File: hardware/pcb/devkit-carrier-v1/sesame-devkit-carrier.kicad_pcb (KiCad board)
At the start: 2 copper layers, 70 x 58 mm, 24 parts, among them J1 DevKit L, J2 DevKit R, J3 OLED, J4 IO, J5 IO2, J6 XT30PW-M, SW1 Switch, U1 Pololu D24V50F5

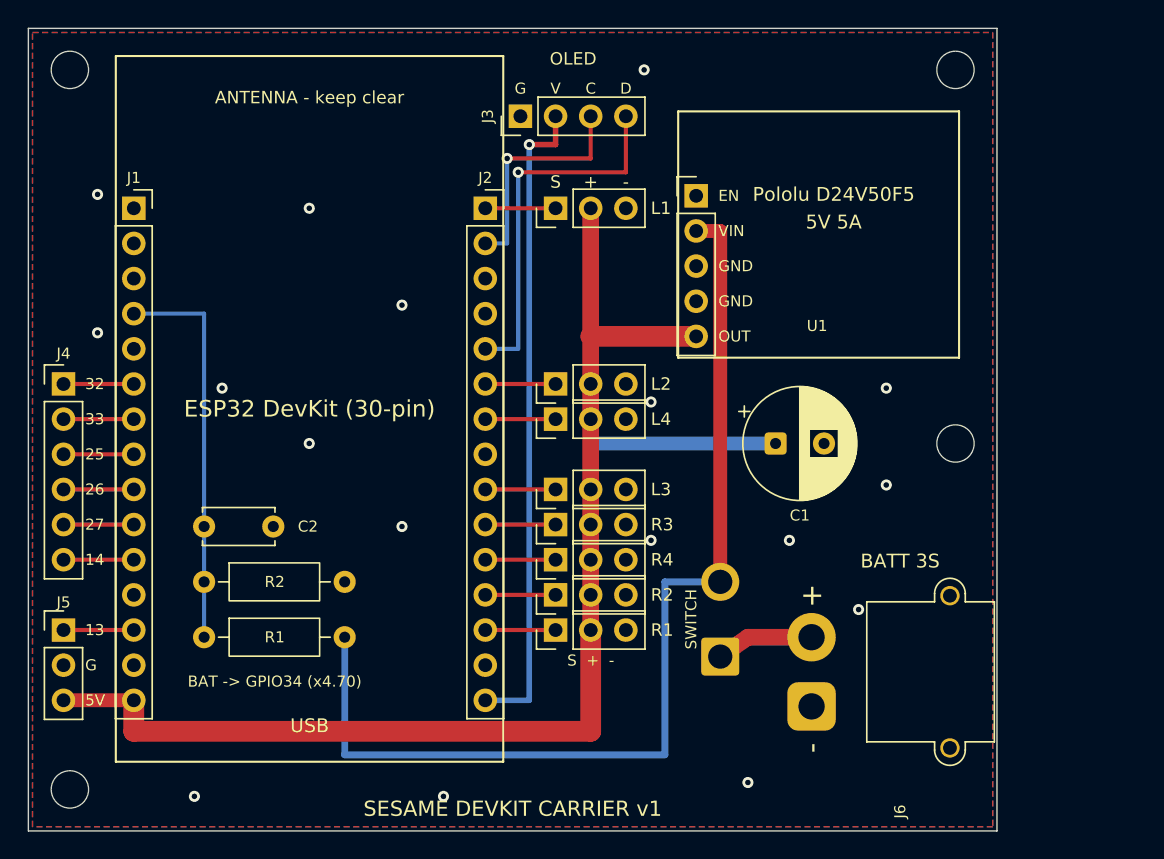
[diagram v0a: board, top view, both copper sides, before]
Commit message: Carrier PCB: 80x42 layout, DevKit USB flush with board edge
DevKit now lies along the board with its micro-USB at the left edge for
flashing; servo headers sit directly under their DevKit pins, spare I/O and
OLED headers along the top edge, power section at the right end.

Co-Authored-By: Claude Opus 5.5 <noreply@anthropic.com>
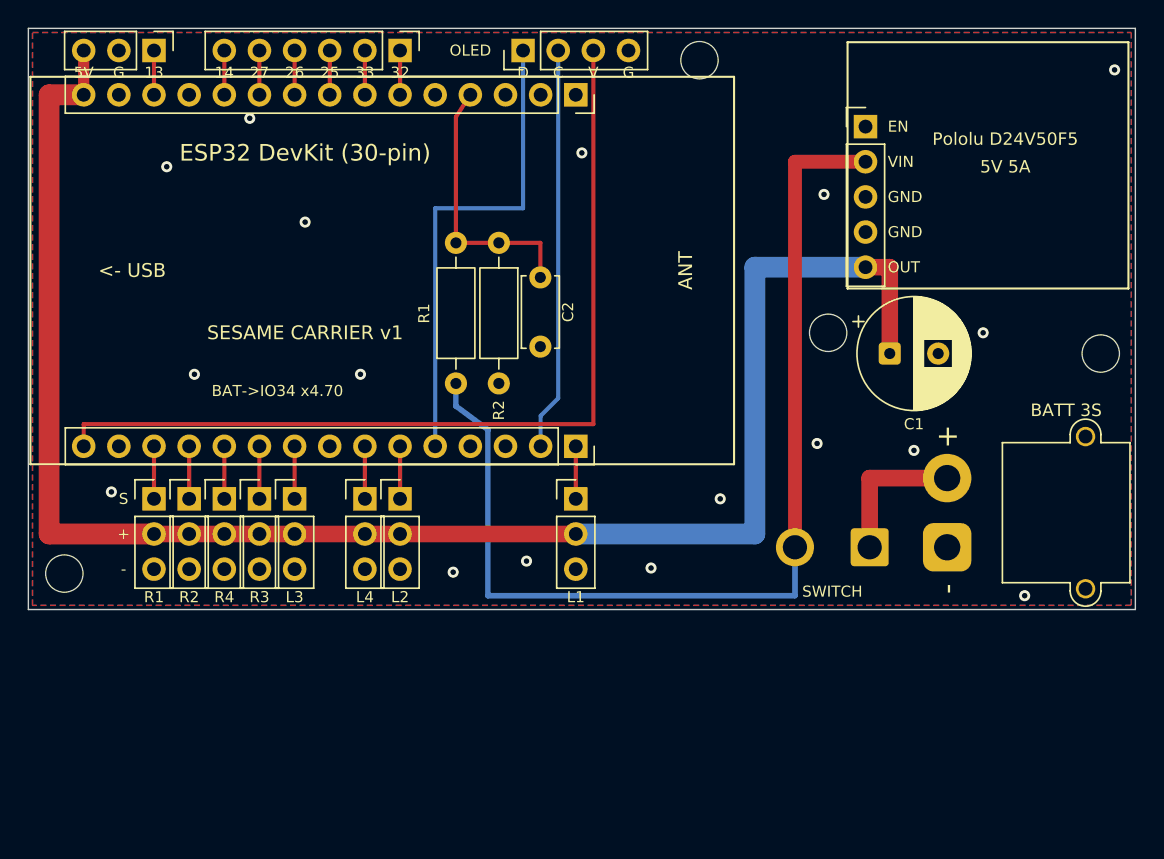
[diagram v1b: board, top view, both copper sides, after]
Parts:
- moved H2 74.0 mm to (2.60, 39.4)
- moved H3 64.0 mm to (57.8, 22.0)
- moved H1 45.5 mm to (48.5, 2.30)
- moved J5 42.4 mm to (9.08, 1.60), turned to -90 degrees
- moved J4 34.2 mm to (26.9, 1.60), turned to -90 degrees
- moved J1 33.0 mm to (39.6, 4.80), turned to -90 degrees
- moved R2 32.5 mm to (34.0, 15.5), turned to -90 degrees
- moved S8 30.5 mm to (9.08, 34.0), turned to 0 degrees
- moved C2 30.2 mm to (37.0, 18.0), turned to -90 degrees
- moved S7 27.4 mm to (11.6, 34.0), turned to 0 degrees
- moved R1 25.8 mm to (30.9, 25.7), turned to 90 degrees
- moved S6 24.3 mm to (14.2, 34.0), turned to 0 degrees
- moved S5 21.5 mm to (16.7, 34.0), turned to 0 degrees
- moved S1 21.1 mm to (39.6, 34.0), turned to 0 degrees
- moved S4 18.9 mm to (19.2, 34.0), turned to 0 degrees
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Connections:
- J3 pad 1: GND -> SDA
- J3 pad 2: +3V3 -> SCL
- J3 pad 3: SCL -> +3V3
- J3 pad 4: SDA -> GND
- R1 pad 1: BAT_SENSE -> VBAT_SW
- R1 pad 2: VBAT_SW -> BAT_SENSE
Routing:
- net +5V: track 100.9 -> 123.7 mm
- net +3V3: track 47.3 -> 65.4 mm, vias 1 -> 0
- net SCL: track 16.8 -> 29.1 mm, vias 1 -> 0
- net BAT_SENSE: track 28.5 -> 19.6 mm
- net SDA: track 27.0 -> 35.0 mm, vias 1 -> 0
- net VBAT: track 7.04 -> 10.6 mm
- net D33: track 5.08 -> 3.20 mm
- net D32: track 5.08 -> 3.20 mm
- net D27: track 5.08 -> 3.20 mm
- net D26: track 5.08 -> 3.20 mm
- net D25: track 5.08 -> 3.20 mm
- net D14: track 5.08 -> 3.20 mm
- net D13: track 5.08 -> 3.20 mm
- net D4: track 5.08 -> 3.80 mm
- net D23: track 5.08 -> 3.80 mm
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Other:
- board size 70 x 58 mm -> 80 x 42 mm
- board text added: "<- USB"
- board text added: "ANT"
- board text added: "BAT->IO34 x4.70"
- board text added: "SESAME CARRIER v1"
- board text removed: "ANTENNA - keep clear"
- board text removed: "BAT -> GPIO34 (x4.70)"
- board text removed: "S + -"
- board text removed: "SESAME DEVKIT CARRIER v1"
- board text removed: "USB"

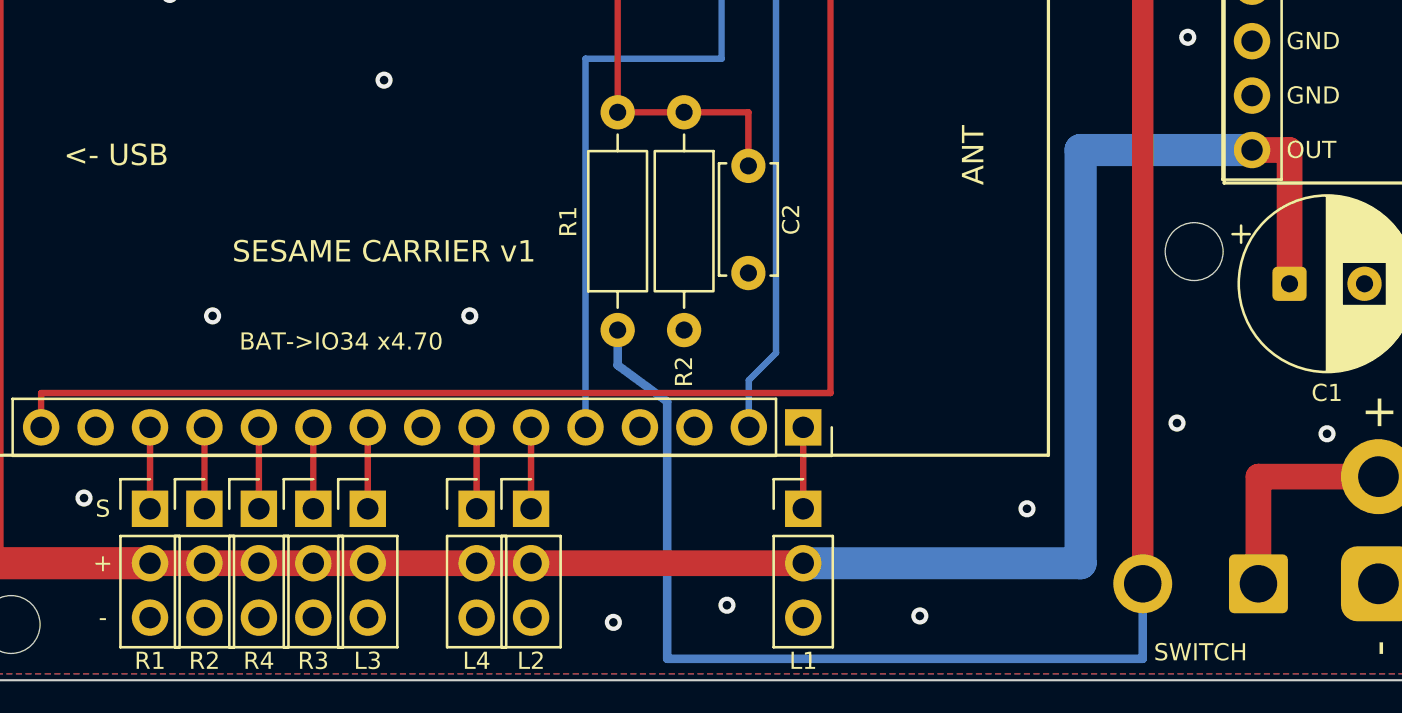
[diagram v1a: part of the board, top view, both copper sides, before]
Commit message: Carrier PCB review fixes: 22k sense resistor, 2mm servo 5V path
R2 27k -> 22k keeps a full 3S pack (12.6 V) at 2.27 V on GPIO34, inside
the ESP32 ADC's accurate range. Servo 5V rail and regulator feed widened
to 2.0 mm for peak servo current.

Co-Authored-By: Claude Opus 5.5 <noreply@anthropic.com>
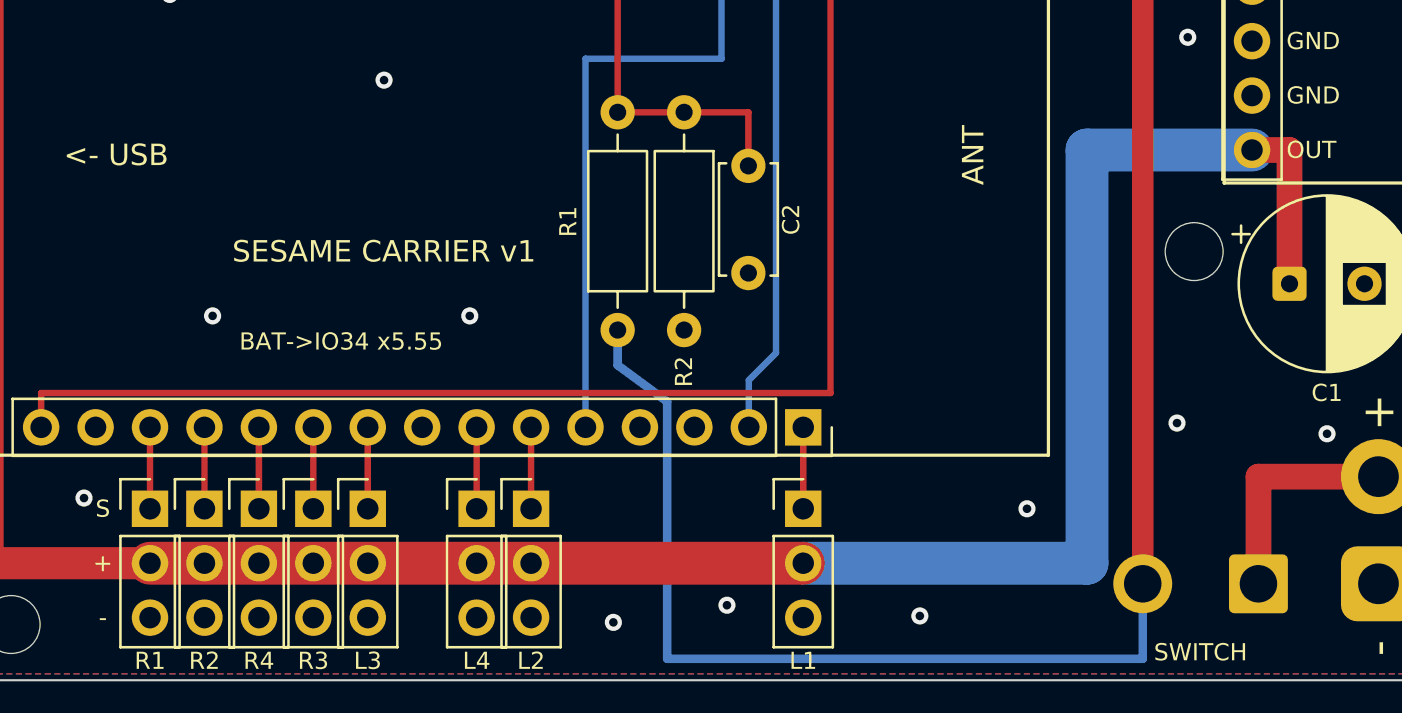
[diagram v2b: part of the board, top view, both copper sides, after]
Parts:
- R2: value 27k -> 22k
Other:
- board text added: "BAT->IO34 x5.55"
- board text removed: "BAT->IO34 x4.70"

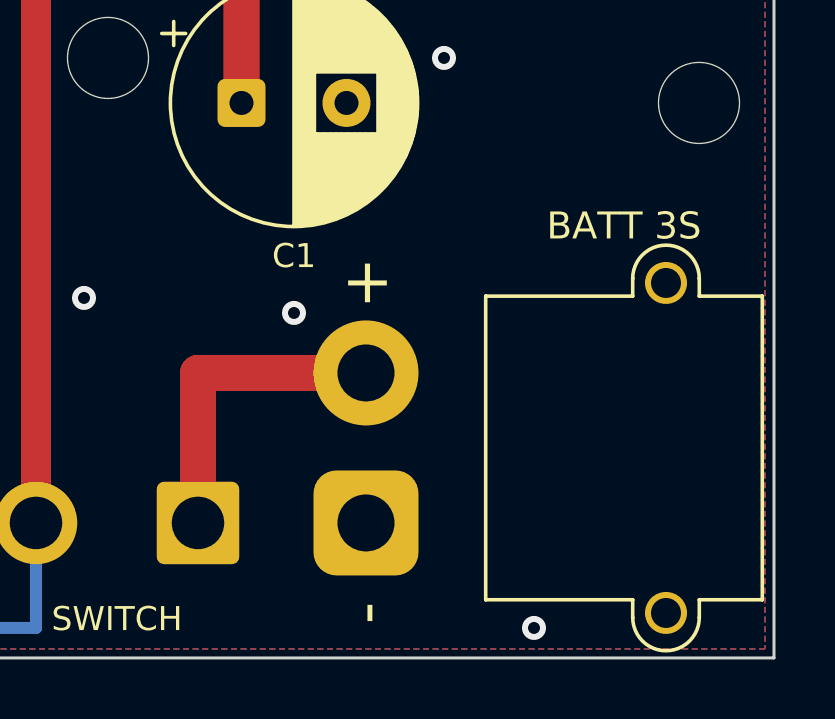
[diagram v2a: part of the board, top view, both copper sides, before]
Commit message: Carrier PCB: replace XT30 with battery pigtail solder pads
Co-Authored-By: Claude Opus 5.5 <noreply@anthropic.com>
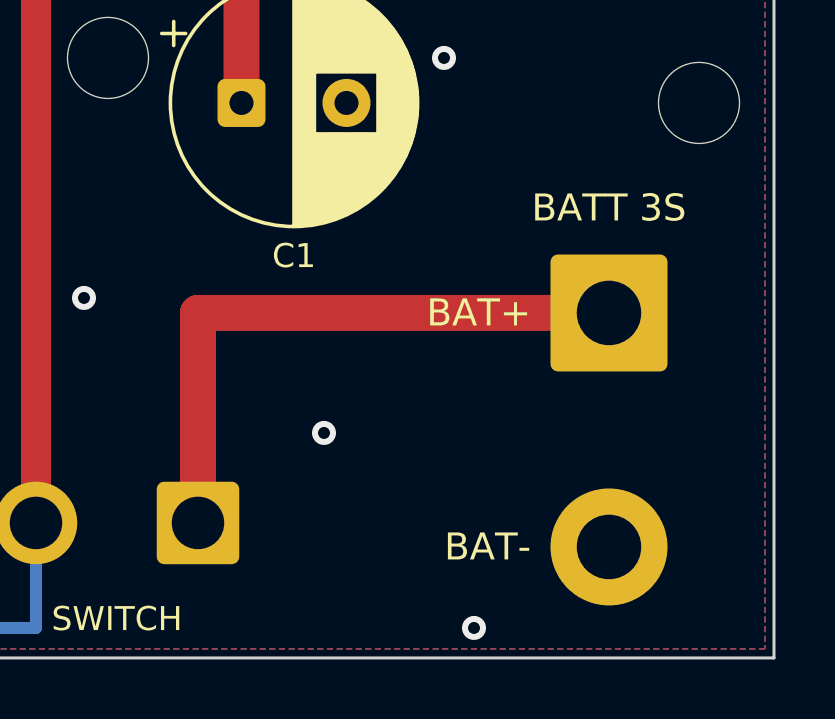
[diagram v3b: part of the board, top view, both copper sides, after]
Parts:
- J6: value XT30PW-M -> Battery pigtail; footprint AMASS_XT30PW-M_1x02_P2.50mm_Horizontal -> SolderWire-1.5sqmm_1x02_P7.8mm_D1.7mm_OD3.9mm
- moved J6 10.7 mm to (74.5, 30.5)
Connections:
- J6 pad 1: GND -> VBAT
- J6 pad 2: VBAT -> GND
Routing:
- net VBAT: track 10.6 -> 20.7 mm
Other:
- board text added: "BAT+"
- board text added: "BAT-"

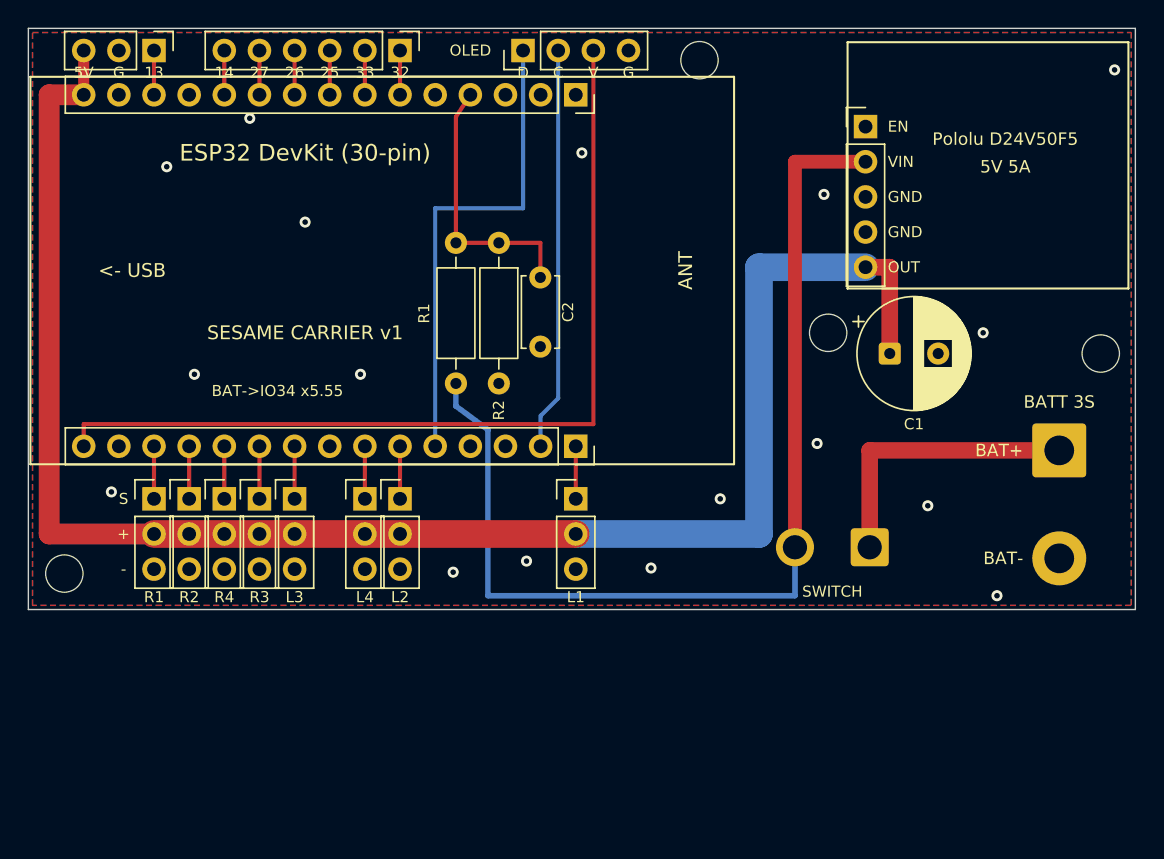
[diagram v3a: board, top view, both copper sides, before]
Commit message: Carrier PCB: antenna slot and clearance zone
Cut a slot under the ESP32 antenna and move the regulator, bulk cap,
battery pads, switch pads and mounting holes to x >= 56 so nothing sits
within ~8 mm of the antenna end, per Espressif placement guidance.

Co-Authored-By: Claude Opus 5.5 <noreply@anthropic.com>
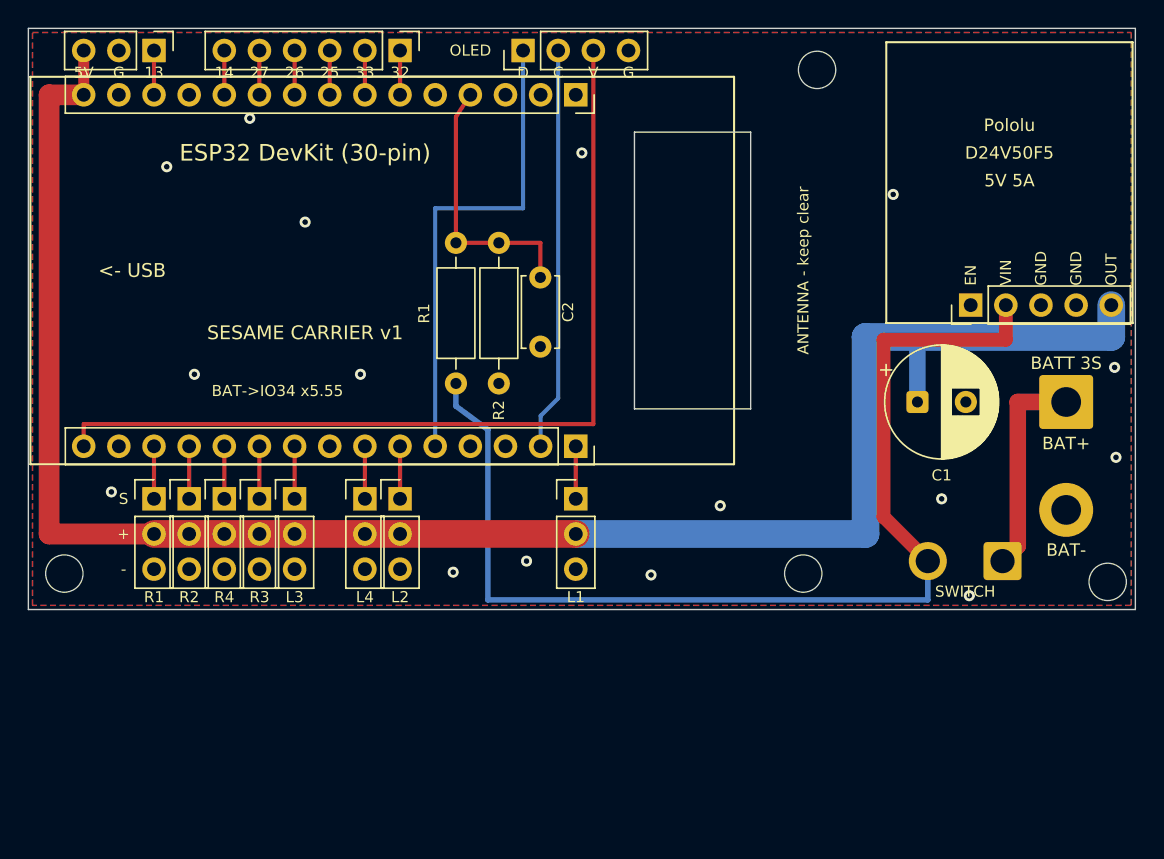
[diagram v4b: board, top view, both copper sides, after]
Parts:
- moved H2 65.5 mm to (57.0, 3.00)
- moved H1 59.0 mm to (2.60, 39.4)
- moved H3 17.5 mm to (56.0, 39.4)
- moved H4 16.5 mm to (78.0, 40.0)
- moved U1 15.0 mm to (68.1, 20.0), turned to 90 degrees
- moved SW1 9.65 mm to (70.4, 38.5)
- moved C1 4.03 mm to (64.2, 27.0)
- moved J6 3.54 mm to (75.0, 27.0)
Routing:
- net +5V: track 123.7 -> 135.4 mm
- net VBAT: track 20.7 -> 15.5 mm
- net VBAT_SW: track 75.2 -> 80.1 mm
- net GND: vias 17 -> 16
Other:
- outline, holes or cut-outs redrawn
- board text added: "ANTENNA - keep clear"
- board text added: "D24V50F5"
- board text added: "Pololu"
- board text removed: "ANT"
- board text removed: "Pololu D24V50F5"
